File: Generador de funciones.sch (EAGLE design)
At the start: 40 parts, among them IC1 ICL8038, IC2 TL084P, IC3 LF353N

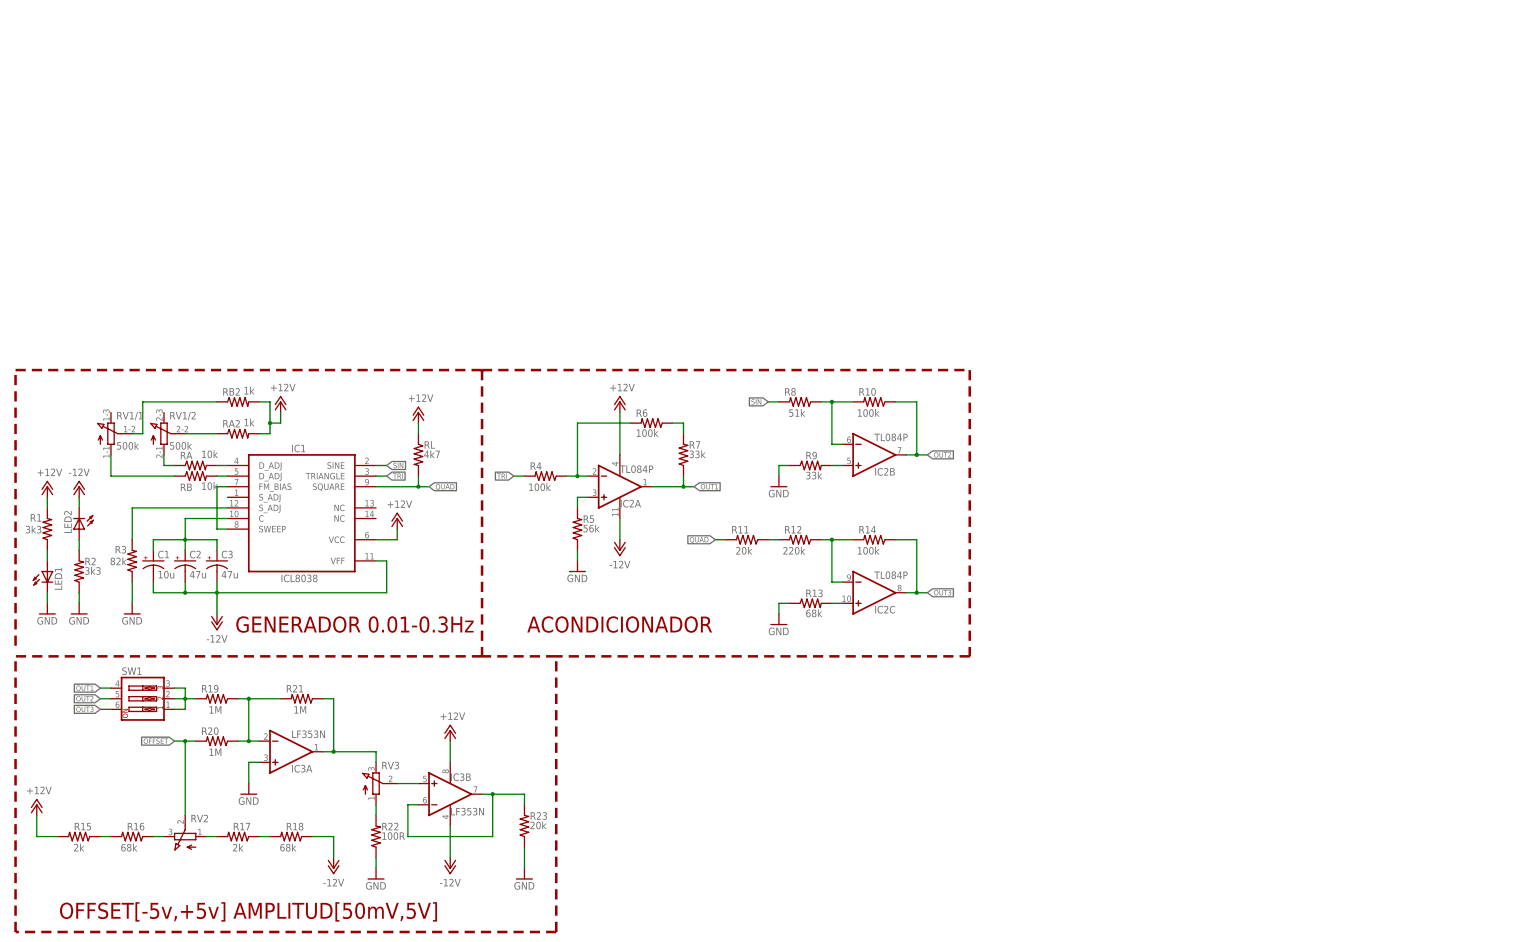
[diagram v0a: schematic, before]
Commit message: Terminado SCH. Andersson Inicia BRD
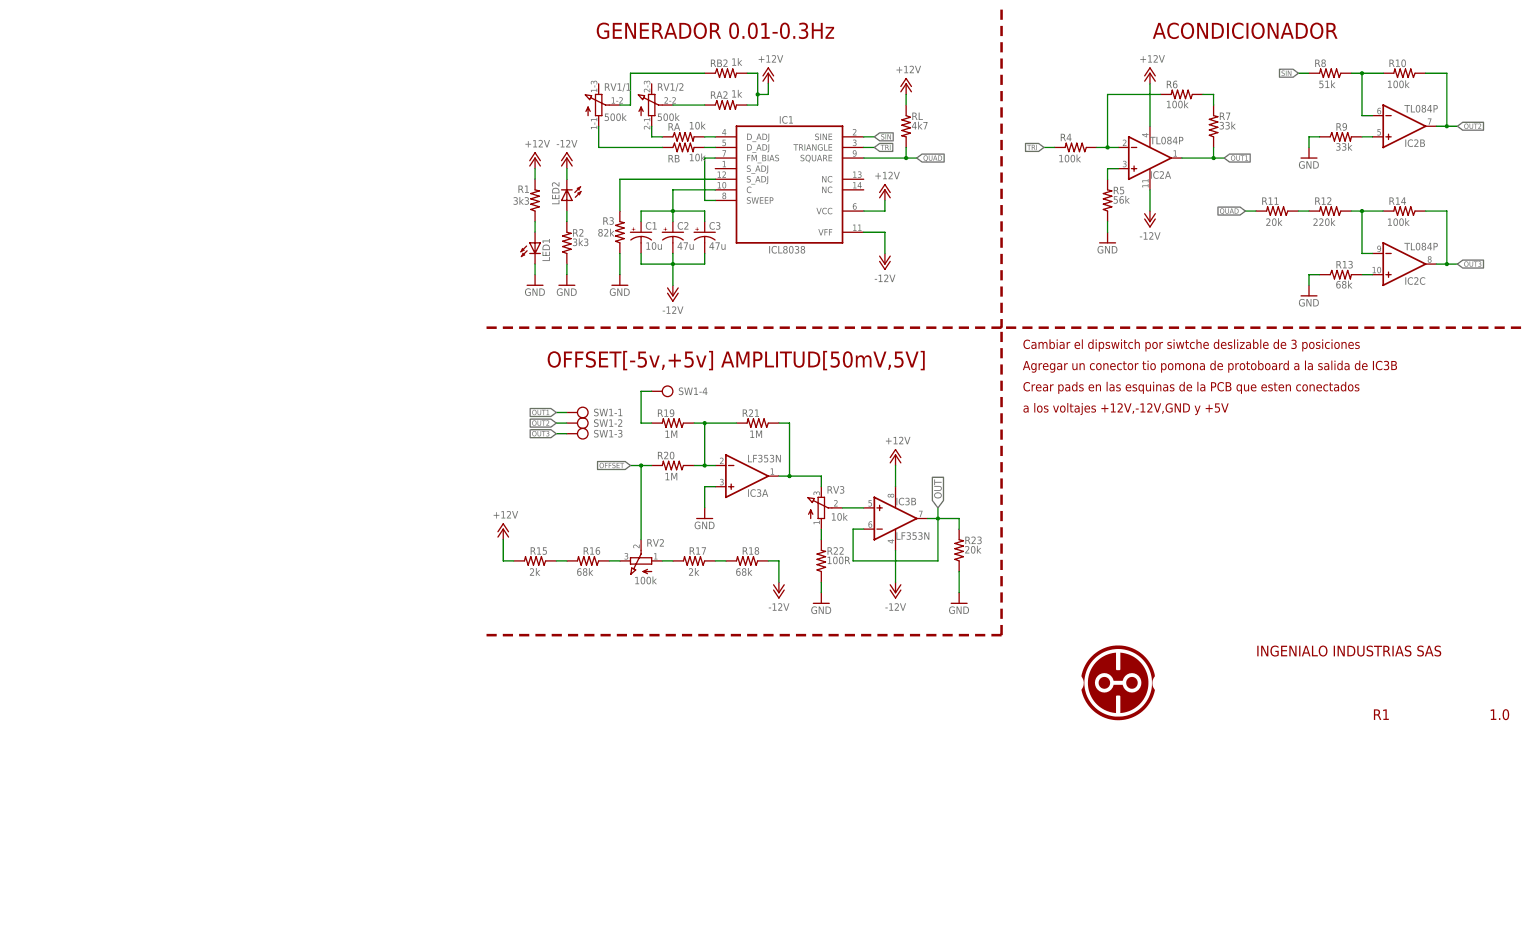
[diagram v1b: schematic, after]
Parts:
- added U$1: LOGO_REDUCIDO, Ingenialo_logos:LOGO_REDUCIDO
- RV2: value (none) -> 100k
- RV3: value (none) -> 10k
- SW1: device special:SW_DIP-3 -> con-ptr500:AK500/4
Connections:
- net N$29 renamed OUT
- net N$20: now also SW1-4.KL; no longer SW1.1, SW1.2, SW1.3
- net OUT1: now also SW1-1.KL; no longer SW1.4
- net OUT2: now also SW1-2.KL; no longer SW1.5
- net OUT3: now also SW1-3.KL; no longer SW1.6
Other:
- note added: "1.0"
- note added: "Agregar un conector tio pomona de protoboard a la salida de IC3B"
- note added: "Cambiar el dipswitch por siwtche deslizable de 3 posiciones"
- note added: "Crear pads en las esquinas de la PCB que esten conectados"
- note added: "INGENIALO INDUSTRIAS SAS"
- note added: "R1"
- note added: "a los voltajes +12V,-12V,GND y +5V"
- moved on the sheet: C1, C2, C3, IC1, IC2A, IC2B, IC2C, IC3A, IC3B, LED1, LED2, R1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

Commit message: Terminado Ubicacion de componentes. Inicio del ruteo
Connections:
- net +12V: now also LED1.A; no longer R1.2
- net GND: now also R1.1; no longer LED1.C
- net N$10: now also LED1.C, R1.2; no longer LED1.A, R1.1
- net OUT1: now also SW1-3.KL; no longer SW1-1.KL
- net OUT3: now also SW1-1.KL; no longer SW1-3.KL
- net SIN: now also R4.2; no longer R8.2
- net TRI: now also R8.2; no longer R4.2
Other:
- note removed: "Agregar un conector tio pomona de protoboard a la salida de IC3B"
- note removed: "Cambiar el dipswitch por siwtche deslizable de 3 posiciones"
- note removed: "Crear pads en las esquinas de la PCB que esten conectados"
- note removed: "a los voltajes +12V,-12V,GND y +5V"
- moved on the sheet: LED1, R1
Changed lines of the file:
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@@
 <text x="218.44" y="5.08" size="2.54" layer="94" ratio="10">R1</text>
 <text x="246.38" y="5.08" size="2.54" layer="94" ratio="10">1.0</text>
-<text x="134.62" y="93.98" size="2.1844" layer="94">Cambiar el dipswitch por siwtche deslizable de 3 posiciones</text>
-<text x="134.62" y="88.9" size="2.1844" layer="94">Agregar un conector tio pomona de protoboard a la salida de IC3B</text>
-<text x="134.62" y="83.82" size="2.1844" layer="94">Crear pads en las esquinas de la PCB que esten conectados</text>
-<text x="134.62" y="78.74" size="2.1844" layer="94">a los voltajes +12V,-12V,GND y +5V</text>
 </plain>
 <instances>
@@
 <attribute name="VALUE" x="35.56" y="106.68" size="1.778" layer="96"/>
 </instance>
-<instance part="LED1" gate="G$1" x="17.78" y="119.38"/>
+<instance part="LED1" gate="G$1" x="17.78" y="132.08"/>
 <instance part="LED2" gate="G$1" x="25.4" y="129.54" rot="R180"/>
 <instance part="RB2" gate="G$1" x="63.5" y="160.02" smashed="yes">
@@
 <attribute name="VALUE" x="104.14" y="160.02" size="1.778" layer="96"/>
 </instance>
-<instance part="R1" gate="G$1" x="17.78" y="129.54" smashed="yes" rot="R90">
-<attribute name="NAME" x="16.51" y="133.1214" size="1.778" layer="95" rot="R180"/>
-<attribute name="VALUE" x="16.51" y="130.302" size="1.778" layer="96" rot="R180"/>
+<instance part="R1" gate="G$1" x="17.78" y="119.38" smashed="yes" rot="R90">
+<attribute name="NAME" x="16.51" y="122.9614" size="1.778" layer="95" rot="R180"/>
+<attribute name="VALUE" x="16.51" y="120.142" size="1.778" layer="96" rot="R180"/>
 </instance>
 <instance part="R2" gate="G$1" x="25.4" y="119.38" smashed="yes" rot="R90">
@@
 </segment>
 <segment>
-<pinref part="LED1" gate="G$1" pin="C"/>
-<pinref part="GND2" gate="1" pin="GND"/>
-<wire x1="17.78" y1="114.3" x2="17.78" y2="111.76" width="0.1524" layer="91"/>
-</segment>
-<segment>
 <pinref part="R2" gate="G$1" pin="1"/>
 <pinref part="GND3" gate="1" pin="GND"/>
@@
 <pinref part="GND9" gate="1" pin="GND"/>
 <wire x1="119.38" y1="40.64" x2="119.38" y2="35.56" width="0.1524" layer="91"/>
+</segment>
+<segment>
+<pinref part="R1" gate="G$1" pin="1"/>
+<pinref part="GND2" gate="1" pin="GND"/>
+<wire x1="17.78" y1="114.3" x2="17.78" y2="111.76" width="0.1524" layer="91"/>
 </segment>
 </net>
@@
 </segment>
 <segment>
-<pinref part="P+4" gate="1" pin="+12V"/>
-<pinref part="R1" gate="G$1" pin="2"/>
-<wire x1="17.78" y1="137.16" x2="17.78" y2="134.62" width="0.1524" layer="91"/>
-</segment>
-<segment>
 <pinref part="P+5" gate="1" pin="+12V"/>
 <pinref part="IC2" gate="P" pin="V+"/>
@@
 <pinref part="IC3" gate="P" pin="V+"/>
 <wire x1="104.14" y1="66.04" x2="104.14" y2="60.96" width="0.1524" layer="91"/>
+</segment>
+<segment>
+<pinref part="LED1" gate="G$1" pin="A"/>
+<pinref part="P+4" gate="1" pin="+12V"/>
+<wire x1="17.78" y1="134.62" x2="17.78" y2="137.16" width="0.1524" layer="91"/>
 </segment>
 </net>
@@
 </segment>
 <segment>
+<pinref part="R4" gate="G$1" pin="2"/>
+<wire x1="142.24" y1="142.24" x2="139.7" y2="142.24" width="0.1524" layer="91"/>
+<label x="139.7" y="142.24" size="1.27" layer="95" rot="R180" xref="yes"/>
+</segment>
+</net>
+<net name="TRI" class="0">
+<segment>
+<pinref part="IC1" gate="G$1" pin="TRIANGLE"/>
+<wire x1="96.52" y1="142.24" x2="99.06" y2="142.24" width="0.1524" layer="91"/>
+<label x="99.06" y="142.24" size="1.27" layer="95" xref="yes"/>
+</segment>
+<segment>
 <pinref part="R8" gate="G$1" pin="2"/>
 <wire x1="203.2" y1="160.02" x2="200.66" y2="160.02" width="0.1524" layer="91"/>
 <label x="200.66" y="160.02" size="1.27" layer="95" rot="R180" xref="yes"/>
-</segment>
-</net>
-<net name="TRI" class="0">
-<segment>
-<pinref part="IC1" gate="G$1" pin="TRIANGLE"/>
-<wire x1="96.52" y1="142.24" x2="99.06" y2="142.24" width="0.1524" layer="91"/>
-<label x="99.06" y="142.24" size="1.27" layer="95" xref="yes"/>
-</segment>
-<segment>
-<pinref part="R4" gate="G$1" pin="2"/>
-<wire x1="142.24" y1="142.24" x2="139.7" y2="142.24" width="0.1524" layer="91"/>
-<label x="139.7" y="142.24" size="1.27" layer="95" rot="R180" xref="yes"/>
 </segment>
 </net>
@@
 </segment>
 </net>
-<net name="N$10" class="0">
-<segment>
-<pinref part="R1" gate="G$1" pin="1"/>
-<pinref part="LED1" gate="G$1" pin="A"/>
-<wire x1="17.78" y1="124.46" x2="17.78" y2="121.92" width="0.1524" layer="91"/>
-</segment>
-</net>
 <net name="N$11" class="0">
 <segment>
@@
 </segment>
 <segment>
-<wire x1="25.4" y1="78.74" x2="22.86" y2="78.74" width="0.1524" layer="91"/>
-<label x="22.86" y="78.74" size="1.27" layer="95" rot="R180" xref="yes"/>
-<pinref part="SW1" gate="-1" pin="KL"/>
+<wire x1="25.4" y1="73.66" x2="22.86" y2="73.66" width="0.1524" layer="91"/>
+<label x="22.86" y="73.66" size="1.27" layer="95" rot="R180" xref="yes"/>
+<pinref part="SW1" gate="-3" pin="KL"/>
 </segment>
 </net>
@@
 <net name="OUT3" class="0">
 <segment>
-<wire x1="25.4" y1="73.66" x2="22.86" y2="73.66" width="0.1524" layer="91"/>
-<label x="22.86" y="73.66" size="1.27" layer="95" rot="R180" xref="yes"/>
-<pinref part="SW1" gate="-3" pin="KL"/>
-</segment>
-<segment>
 <pinref part="IC2" gate="C" pin="OUT"/>
 <wire x1="233.68" y1="114.3" x2="236.22" y2="114.3" width="0.1524" layer="91"/>
@@
 <wire x1="236.22" y1="114.3" x2="238.76" y2="114.3" width="0.1524" layer="91"/>
 <label x="238.76" y="114.3" size="1.27" layer="95" xref="yes"/>
+</segment>
+<segment>
+<wire x1="25.4" y1="78.74" x2="22.86" y2="78.74" width="0.1524" layer="91"/>
+<label x="22.86" y="78.74" size="1.27" layer="95" rot="R180" xref="yes"/>
+<pinref part="SW1" gate="-1" pin="KL"/>
 </segment>
 </net>
@@
 </segment>
 </net>
+<net name="N$10" class="0">
+<segment>
+<pinref part="LED1" gate="G$1" pin="C"/>
+<pinref part="R1" gate="G$1" pin="2"/>
+<wire x1="17.78" y1="127" x2="17.78" y2="124.46" width="0.1524" layer="91"/>
+</segment>
+</net>

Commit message: Generado imagenes SCH y BRD
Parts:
- removed U$1: LOGO_REDUCIDO, Ingenialo_logos:LOGO_REDUCIDO
- added FRAME1: A4_HORIZONTAL, Circuitos-Creativos-Estilos:A4_HORIZONTAL
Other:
- note removed: "INGENIALO INDUSTRIAS SAS"
- moved on the sheet: C1, C2, C3, IC1, IC2A, IC2B, IC2C, IC3A, IC3B, LED1, LED2, R1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
